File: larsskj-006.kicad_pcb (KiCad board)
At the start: 2 copper layers, 68.6 x 53.3 mm, 18 parts, among them J1 Barrel_Jack, J2 IDC 16 pin, J3 IDC 16 pin, P1 Power, P2 Analog, P3 Digital, P4 Digital, P5 CONN_01X01, P6 CONN_01X01, P7 CONN_01X01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

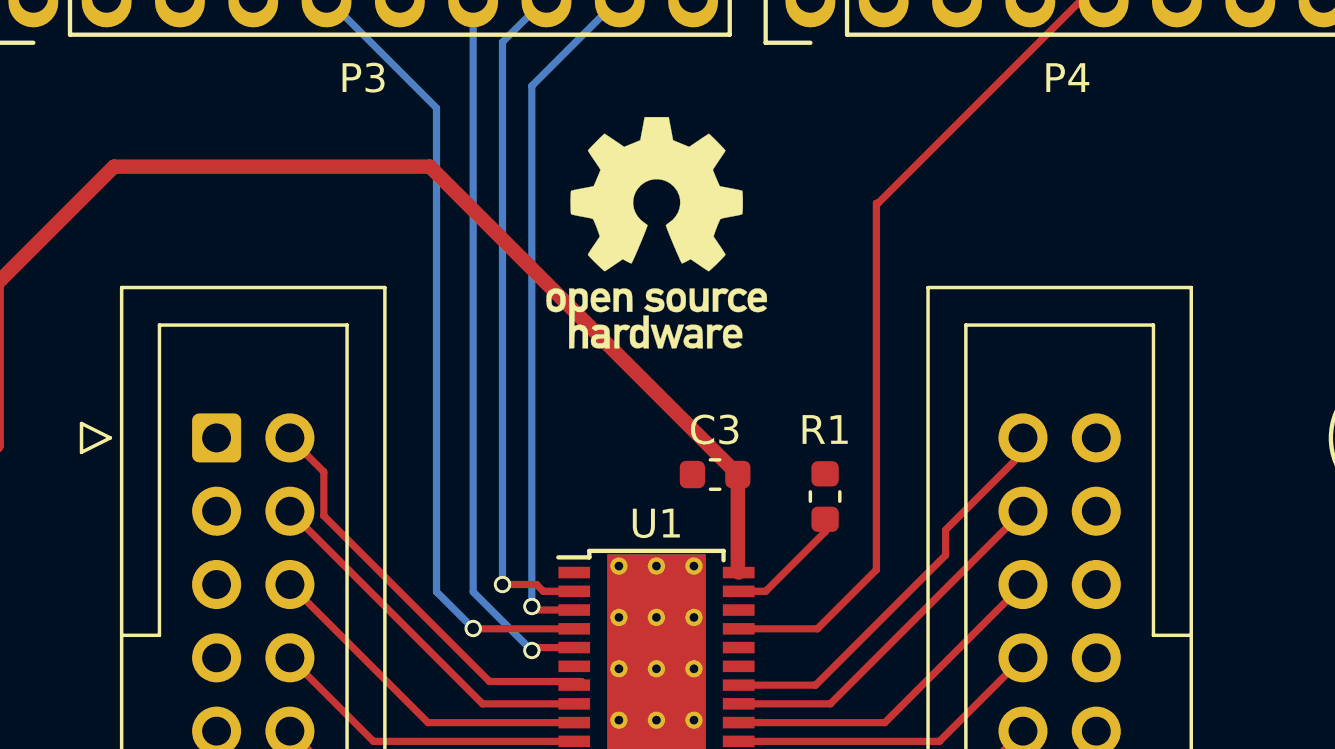
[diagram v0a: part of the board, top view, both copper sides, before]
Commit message: Part numbers added
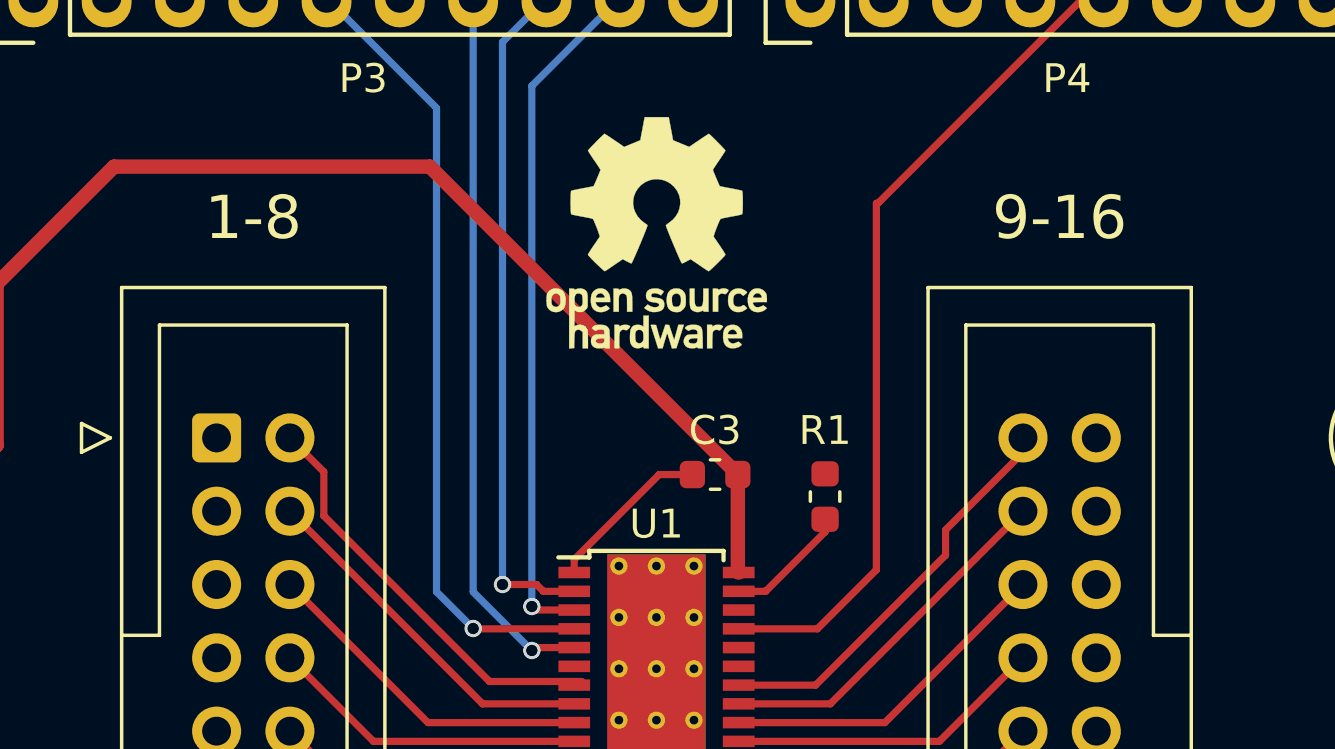
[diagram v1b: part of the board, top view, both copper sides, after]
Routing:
- net GND: track 0.00 -> 5.76 mm
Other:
- board text added: "1-8"
- board text added: "9-16"
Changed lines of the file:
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@@
   (general
     (thickness 1.6)
-    (drawings 28)
-    (tracks 96)
+    (drawings 30)
+    (tracks 99)
     (zones 0)
     (modules 18)
@@
     (visible_elements FFFFFF7F)
     (pcbplotparams
-      (layerselection 0x00030_80000001)
+      (layerselection 0x010f0_ffffffff)
       (usegerberextensions false)
       (usegerberattributes true)
@@
       (outputformat 1)
       (mirror false)
-      (drillshape 1)
+      (drillshape 0)
       (scaleselection 1)
-      (outputdirectory ""))
+      (outputdirectory "plots/"))
   )
   (net 0 "")
@@
     )
   )
+  (gr_text 9-16 (at 165.354 83.185) (layer F.SilkS)
+    (effects (font (size 1.5 1.5) (thickness 0.3)))
+  )
+  (gr_text 1-8 (at 137.414 83.185) (layer F.SilkS)
+    (effects (font (size 1.5 1.5) (thickness 0.3)))
+  )
   (gr_text larsskj-006-01 (at 151.384 117.729) (layer F.SilkS)
     (effects (font (size 1.5 1.5) (thickness 0.3)))
@@
   (gr_line (start 120.523 82.55) (end 120.523 93.98) (angle 90) (layer Dwgs.User) (width 0.15))
   (gr_line (start 104.648 82.55) (end 120.523 82.55) (angle 90) (layer Dwgs.User) (width 0.15))
+  (segment (start 151.479 92.075) (end 152.6285 92.075) (width 0.25) (layer F.Cu) (net 1))
+  (segment (start 148.534 95.02) (end 151.479 92.075) (width 0.25) (layer F.Cu) (net 1))
+  (segment (start 148.534 95.47) (end 148.534 95.02) (width 0.25) (layer F.Cu) (net 1))
   (segment (start 122.428 118.745) (end 122.428 113.157) (width 0.5) (layer F.Cu) (net 7))
   (segment (start 122.428 113.157) (end 117.856 108.585) (width 0.5) (layer F.Cu) (net 7))
@@
   (segment (start 143.469 100.67) (end 138.684 95.885) (width 0.25) (layer F.Cu) (net 11))
   (segment (start 148.534 100.67) (end 143.469 100.67) (width 0.25) (layer F.Cu) (net 11))
-  (segment (start 138.777 108.492) (end 138.684 108.585) (width 0.25) (layer B.Cu) (net 16))
   (segment (start 148.534 101.342) (end 148.205 101.342) (width 0.25) (layer F.Cu) (net 12))
   (segment (start 141.579 101.32) (end 138.684 98.425) (width 0.25) (layer F.Cu) (net 12))
@@
   (segment (start 141.459 103.27) (end 138.684 106.045) (width 0.25) (layer F.Cu) (net 15))
   (segment (start 148.534 103.27) (end 141.459 103.27) (width 0.25) (layer F.Cu) (net 15))
+  (segment (start 138.777 108.492) (end 138.684 108.585) (width 0.25) (layer B.Cu) (net 16))
   (segment (start 143.349 103.92) (end 138.684 108.585) (width 0.25) (layer F.Cu) (net 16))
   (segment (start 148.534 103.92) (end 143.349 103.92) (width 0.25) (layer F.Cu) (net 16))
